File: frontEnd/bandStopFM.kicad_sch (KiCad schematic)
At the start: 18 parts, among them U301 BGS12P2L6E6327XTSA1, U302 BGS12P2L6E6327XTSA1

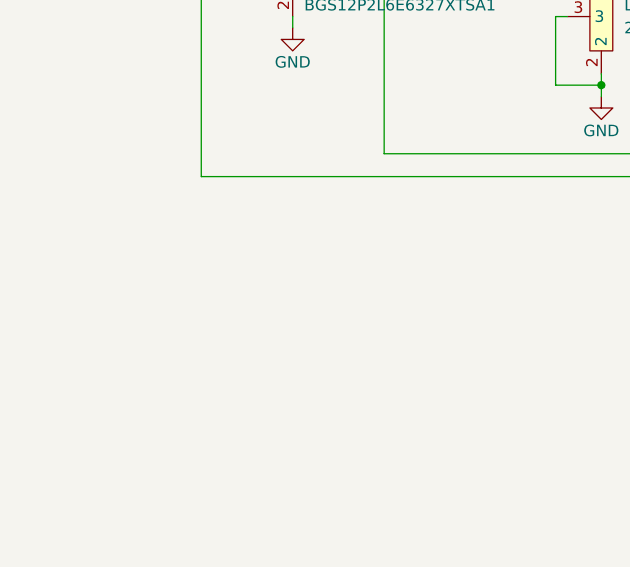
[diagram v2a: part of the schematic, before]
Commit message: add leds for each filter block
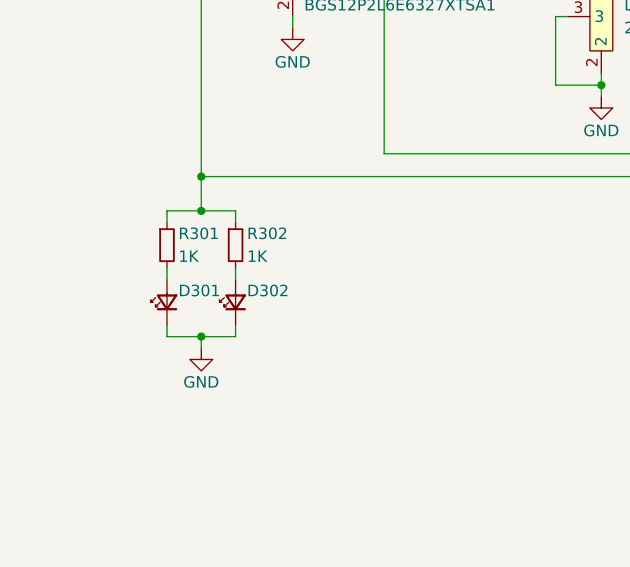
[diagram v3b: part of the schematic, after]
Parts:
- added D301, D302: LED_Small, LED_SMD:LED_0805_2012Metric, symbol Device:LED_Small
- added R301, R302: 1K, Resistor_SMD:R_0805_2012Metric, symbol Device:R_Small
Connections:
- net FILTER_ENABLE: now also R301.1, R302.1
- net GND: now also D301.1 (K), D302.1 (K)
- new net: D301.2 (A), R301.2
- new net: D302.2 (A), R302.2
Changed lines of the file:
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@@
 (kicad_sch (version 20211123) (generator eeschema)
   (paper "A4")
+  (junction (at 58.42 125.73) (diameter 0) (color 0 0 0 0)
+  )
+  (junction (at 58.42 111.76) (diameter 0) (color 0 0 0 0)
+  )
   (junction (at 127 76.2) (diameter 0) (color 0 0 0 0)
   )
@@
   (junction (at 193.04 76.2) (diameter 0) (color 0 0 0 0)
   )
+  (junction (at 58.42 107.95) (diameter 0) (color 0 0 0 0)
+  )
   (junction (at 45.72 167.64) (diameter 0) (color 0 0 0 0)
   )
@@
     (stroke (width 0) (type default) (color 0 0 0 0))
   )
+  (wire (pts (xy 62.23 124.46) (xy 62.23 125.73))
+    (stroke (width 0) (type default) (color 0 0 0 0))
+  )
   (wire (pts (xy 135.89 97.79) (xy 135.89 99.06))
     (stroke (width 0) (type default) (color 0 0 0 0))
@@
     (stroke (width 0) (type default) (color 0 0 0 0))
   )
+  (wire (pts (xy 54.61 125.73) (xy 58.42 125.73))
+    (stroke (width 0) (type default) (color 0 0 0 0))
+  )
   (wire (pts (xy 135.89 82.55) (xy 135.89 83.82))
     (stroke (width 0) (type default) (color 0 0 0 0))
@@
     (stroke (width 0) (type default) (color 0 0 0 0))
   )
+  (wire (pts (xy 54.61 113.03) (xy 54.61 111.76))
+    (stroke (width 0) (type default) (color 0 0 0 0))
+  )
   (wire (pts (xy 119.38 86.36) (xy 119.38 87.63))
     (stroke (width 0) (type default) (color 0 0 0 0))
@@
     (stroke (width 0) (type default) (color 0 0 0 0))
   )
+  (wire (pts (xy 58.42 111.76) (xy 62.23 111.76))
+    (stroke (width 0) (type default) (color 0 0 0 0))
+  )
   (wire (pts (xy 68.58 90.17) (xy 68.58 91.44))
     (stroke (width 0) (type default) (color 0 0 0 0))
@@
     (stroke (width 0) (type default) (color 0 0 0 0))
   )
+  (wire (pts (xy 58.42 125.73) (xy 58.42 127))
+    (stroke (width 0) (type default) (color 0 0 0 0))
+  )
   (wire (pts (xy 227.33 69.85) (xy 227.33 71.12))
     (stroke (width 0) (type default) (color 0 0 0 0))
@@
     (stroke (width 0) (type default) (color 0 0 0 0))
   )
+  (wire (pts (xy 54.61 118.11) (xy 54.61 119.38))
+    (stroke (width 0) (type default) (color 0 0 0 0))
+  )
+  (wire (pts (xy 62.23 118.11) (xy 62.23 119.38))
+    (stroke (width 0) (type default) (color 0 0 0 0))
+  )
   (wire (pts (xy 135.89 96.52) (xy 135.89 97.79))
     (stroke (width 0) (type default) (color 0 0 0 0))
@@
     (stroke (width 0) (type default) (color 0 0 0 0))
   )
+  (wire (pts (xy 54.61 124.46) (xy 54.61 125.73))
+    (stroke (width 0) (type default) (color 0 0 0 0))
+  )
   (wire (pts (xy 97.79 90.17) (xy 97.79 97.79))
     (stroke (width 0) (type default) (color 0 0 0 0))
@@
     (stroke (width 0) (type default) (color 0 0 0 0))
   )
+  (wire (pts (xy 54.61 111.76) (xy 58.42 111.76))
+    (stroke (width 0) (type default) (color 0 0 0 0))
+  )
   (wire (pts (xy 127 76.2) (xy 135.89 76.2))
     (stroke (width 0) (type default) (color 0 0 0 0))
@@
     (stroke (width 0) (type default) (color 0 0 0 0))
   )
+  (wire (pts (xy 58.42 125.73) (xy 62.23 125.73))
+    (stroke (width 0) (type default) (color 0 0 0 0))
+  )
   (wire (pts (xy 102.87 96.52) (xy 102.87 97.79))
     (stroke (width 0) (type default) (color 0 0 0 0))
@@
     (stroke (width 0) (type default) (color 0 0 0 0))
   )
+  (wire (pts (xy 58.42 107.95) (xy 58.42 111.76))
+    (stroke (width 0) (type default) (color 0 0 0 0))
+  )
   (wire (pts (xy 78.74 81.28) (xy 78.74 105.41))
     (stroke (width 0) (type default) (color 0 0 0 0))
@@
   )
   (wire (pts (xy 237.49 107.95) (xy 58.42 107.95))
+    (stroke (width 0) (type default) (color 0 0 0 0))
+  )
+  (wire (pts (xy 62.23 111.76) (xy 62.23 113.03))
     (stroke (width 0) (type default) (color 0 0 0 0))
   )
@@
     )
     (pin "1")
+  )
+  (symbol (lib_id "Device:R_Small") (at 54.61 115.57 0) (unit 1)
+    (in_bom yes) (on_board yes)
+    (property "Reference" "R301" (id 0) (at 55.88 114.3 0)
+      (effects (font (size 1.27 1.27)) (justify left))
+    )
+    (property "Value" "1K" (id 1) (at 55.88 116.84 0)
+      (effects (font (size 1.27 1.27)) (justify left))
+    )
+    (property "Footprint" "Resistor_SMD:R_0805_2012Metric" (id 2) (at 54.61 115.57 0)
+      (effects (font (size 1.27 1.27)) hide)
+    )
+    (property "Datasheet" "~" (id 3) (at 54.61 115.57 0)
+      (effects (font (size 1.27 1.27)) hide)
+    )
+    (pin "1")
+    (pin "2")
   )
   (symbol (lib_id "frontEnd:BGS12P2L6E6327XTSA1") (at 233.68 78.74 0) (mirror y) (unit 1)
@@
     (pin "2")
   )
+  (symbol (lib_id "Device:LED_Small") (at 54.61 121.92 90) (unit 1)
+    (in_bom yes) (on_board yes)
+    (property "Reference" "D301" (id 0) (at 55.88 120.65 90)
+      (effects (font (size 1.27 1.27)) (justify right))
+    )
+    (property "Value" "LED_Small" (id 1) (at 57.15 123.1264 90)
+      (effects (font (size 1.27 1.27)) (justify right) hide)
+    )
+    (property "Footprint" "LED_SMD:LED_0805_2012Metric" (id 2) (at 54.61 121.92 90)
+      (effects (font (size 1.27 1.27)) hide)
+    )
+    (property "Datasheet" "~" (id 3) (at 54.61 121.92 90)
+      (effects (font (size 1.27 1.27)) hide)
+    )
+    (pin "1")
+    (pin "2")
+  )
   (symbol (lib_id "Device:C_Small") (at 41.91 171.45 180) (unit 1)
     (in_bom yes) (on_board yes)
@@
     )
     (property "Datasheet" "~" (id 3) (at 135.89 80.01 0)
+      (effects (font (size 1.27 1.27)) hide)
+    )
+    (pin "1")
+    (pin "2")
+  )
+  (symbol (lib_id "Device:LED_Small") (at 62.23 121.92 90) (unit 1)
+    (in_bom yes) (on_board yes)
+    (property "Reference" "D302" (id 0) (at 63.5 120.65 90)
+      (effects (font (size 1.27 1.27)) (justify right))
+    )
+    (property "Value" "LED_Small" (id 1) (at 64.77 123.1264 90)
+      (effects (font (size 1.27 1.27)) (justify right) hide)
+    )
+    (property "Footprint" "LED_SMD:LED_0805_2012Metric" (id 2) (at 62.23 121.92 90)
+      (effects (font (size 1.27 1.27)) hide)
+    )
+    (property "Datasheet" "~" (id 3) (at 62.23 121.92 90)
       (effects (font (size 1.27 1.27)) hide)
     )
@@
       (effects (font (size 1.27 1.27)) hide)
     )
+    (pin "1")
+    (pin "2")
+  )
+  (symbol (lib_id "power:GND") (at 58.42 127 0) (unit 1)
+    (in_bom yes) (on_board yes)
+    (property "Reference" "#PWR?" (id 0) (at 58.42 133.35 0)
+      (effects (font (size 1.27 1.27)) hide)
+    )
+    (property "Value" "GND" (id 1) (at 58.42 130.81 0))
+    (property "Footprint" "" (id 2) (at 58.42 127 0)
+      (effects (font (size 1.27 1.27)) hide)
+    )
+    (property "Datasheet" "" (id 3) (at 58.42 127 0)
+      (effects (font (size 1.27 1.27)) hide)
+    )
+    (pin "1")
+  )
+  (symbol (lib_id "Device:R_Small") (at 62.23 115.57 0) (unit 1)
+    (in_bom yes) (on_board yes)
+    (property "Reference" "R302" (id 0) (at 63.5 114.3 0)
+      (effects (font (size 1.27 1.27)) (justify left))
+    )
+    (property "Value" "1K" (id 1) (at 63.5 116.84 0)
+      (effects (font (size 1.27 1.27)) (justify left))
+    )
+    (property "Footprint" "Resistor_SMD:R_0805_2012Metric" (id 2) (at 62.23 115.57 0)
+      (effects (font (size 1.27 1.27)) hide)
+    )
+    (property "Datasheet" "~" (id 3) (at 62.23 115.57 0)
+      (effects (font (size 1.27 1.27)) hide)
+    )

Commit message: assign footprints, part designators
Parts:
- U301, U302: footprint (none) -> frontEnd:BGS12P2L6E6327XTSA1
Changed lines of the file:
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@@
   (symbol (lib_id "power:GND") (at 201.93 99.06 0) (unit 1)
     (in_bom yes) (on_board yes)
-    (property "Reference" "#PWR?" (id 0) (at 201.93 105.41 0)
+    (property "Reference" "#PWR0156" (id 0) (at 201.93 105.41 0)
       (effects (font (size 1.27 1.27)) hide)
     )
@@
       (effects (font (size 1.27 1.27)) (justify right))
     )
-    (property "Footprint" "" (id 2) (at 233.68 78.74 0)
+    (property "Footprint" "frontEnd:BGS12P2L6E6327XTSA1" (id 2) (at 233.68 78.74 0)
       (effects (font (size 1.27 1.27)) hide)
     )
@@
   (symbol (lib_id "power:GND") (at 119.38 87.63 0) (unit 1)
     (in_bom yes) (on_board yes)
-    (property "Reference" "#PWR?" (id 0) (at 119.38 93.98 0)
+    (property "Reference" "#PWR0148" (id 0) (at 119.38 93.98 0)
       (effects (font (size 1.27 1.27)) hide)
     )
@@
   (symbol (lib_id "power:GND") (at 135.89 99.06 0) (unit 1)
     (in_bom yes) (on_board yes)
-    (property "Reference" "#PWR?" (id 0) (at 135.89 105.41 0)
+    (property "Reference" "#PWR0150" (id 0) (at 135.89 105.41 0)
       (effects (font (size 1.27 1.27)) hide)
     )
@@
   (symbol (lib_id "power:+3V3") (at 227.33 69.85 0) (unit 1)
     (in_bom yes) (on_board yes)
-    (property "Reference" "#PWR?" (id 0) (at 227.33 73.66 0)
+    (property "Reference" "#PWR0155" (id 0) (at 227.33 73.66 0)
       (effects (font (size 1.27 1.27)) hide)
     )
@@
   (symbol (lib_id "power:GND") (at 152.4 87.63 0) (unit 1)
     (in_bom yes) (on_board yes)
-    (property "Reference" "#PWR?" (id 0) (at 152.4 93.98 0)
+    (property "Reference" "#PWR0149" (id 0) (at 152.4 93.98 0)
       (effects (font (size 1.27 1.27)) hide)
     )
@@
   (symbol (lib_id "power:GND") (at 168.91 99.06 0) (unit 1)
     (in_bom yes) (on_board yes)
-    (property "Reference" "#PWR?" (id 0) (at 168.91 105.41 0)
+    (property "Reference" "#PWR0152" (id 0) (at 168.91 105.41 0)
       (effects (font (size 1.27 1.27)) hide)
     )
@@
   (symbol (lib_id "power:GND") (at 227.33 91.44 0) (unit 1)
     (in_bom yes) (on_board yes)
-    (property "Reference" "#PWR?" (id 0) (at 227.33 97.79 0)
+    (property "Reference" "#PWR0154" (id 0) (at 227.33 97.79 0)
       (effects (font (size 1.27 1.27)) hide)
     )
@@
   (symbol (lib_id "power:GND") (at 68.58 91.44 0) (unit 1)
     (in_bom yes) (on_board yes)
-    (property "Reference" "#PWR?" (id 0) (at 68.58 97.79 0)
+    (property "Reference" "#PWR0157" (id 0) (at 68.58 97.79 0)
       (effects (font (size 1.27 1.27)) hide)
     )
@@
   (symbol (lib_id "power:GND") (at 45.72 176.53 0) (unit 1)
     (in_bom yes) (on_board yes)
-    (property "Reference" "#PWR?" (id 0) (at 45.72 182.88 0)
+    (property "Reference" "#PWR0160" (id 0) (at 45.72 182.88 0)
       (effects (font (size 1.27 1.27)) hide)
     )
@@
   (symbol (lib_id "power:+3V3") (at 45.72 166.37 0) (unit 1)
     (in_bom yes) (on_board yes)
-    (property "Reference" "#PWR?" (id 0) (at 45.72 170.18 0)
+    (property "Reference" "#PWR0161" (id 0) (at 45.72 170.18 0)
       (effects (font (size 1.27 1.27)) hide)
     )
@@
   (symbol (lib_id "power:GND") (at 185.42 87.63 0) (unit 1)
     (in_bom yes) (on_board yes)
-    (property "Reference" "#PWR?" (id 0) (at 185.42 93.98 0)
+    (property "Reference" "#PWR0153" (id 0) (at 185.42 93.98 0)
       (effects (font (size 1.27 1.27)) hide)
     )
@@
   (symbol (lib_id "power:GND") (at 102.87 99.06 0) (unit 1)
     (in_bom yes) (on_board yes)
-    (property "Reference" "#PWR?" (id 0) (at 102.87 105.41 0)
+    (property "Reference" "#PWR0151" (id 0) (at 102.87 105.41 0)
       (effects (font (size 1.27 1.27)) hide)
     )
@@
       (effects (font (size 1.27 1.27)) (justify left))
     )
-    (property "Footprint" "" (id 2) (at 62.23 78.74 0)
+    (property "Footprint" "frontEnd:BGS12P2L6E6327XTSA1" (id 2) (at 62.23 78.74 0)
       (effects (font (size 1.27 1.27)) hide)
     )
@@
   (symbol (lib_id "power:+3V3") (at 68.58 69.85 0) (unit 1)
     (in_bom yes) (on_board yes)
-    (property "Reference" "#PWR?" (id 0) (at 68.58 73.66 0)
+    (property "Reference" "#PWR0158" (id 0) (at 68.58 73.66 0)
       (effects (font (size 1.27 1.27)) hide)
     )
@@
   (symbol (lib_id "power:GND") (at 58.42 127 0) (unit 1)
     (in_bom yes) (on_board yes)
-    (property "Reference" "#PWR?" (id 0) (at 58.42 133.35 0)
-      (effects (font (size 1.27 1.27)) hide)
-    )
+    (property "Reference" "#PWR0159" (id 0) (at 58.42 133.35 0)
+      (effects (font (size 1.27 1.27)) hide)
+    )

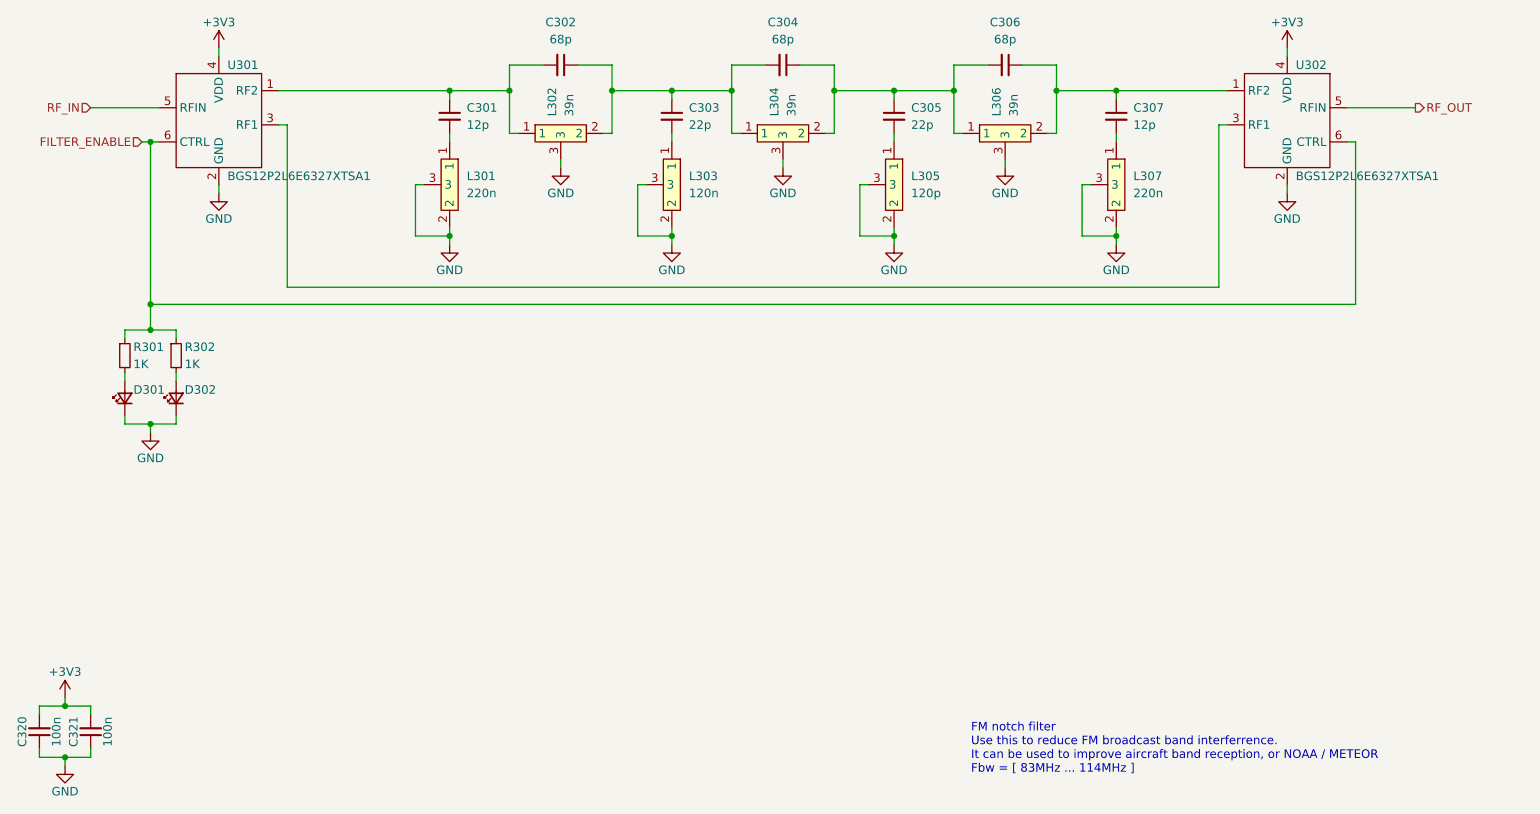
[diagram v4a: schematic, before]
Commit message: convert all embeded filter to plug-in modules, start pcb layout
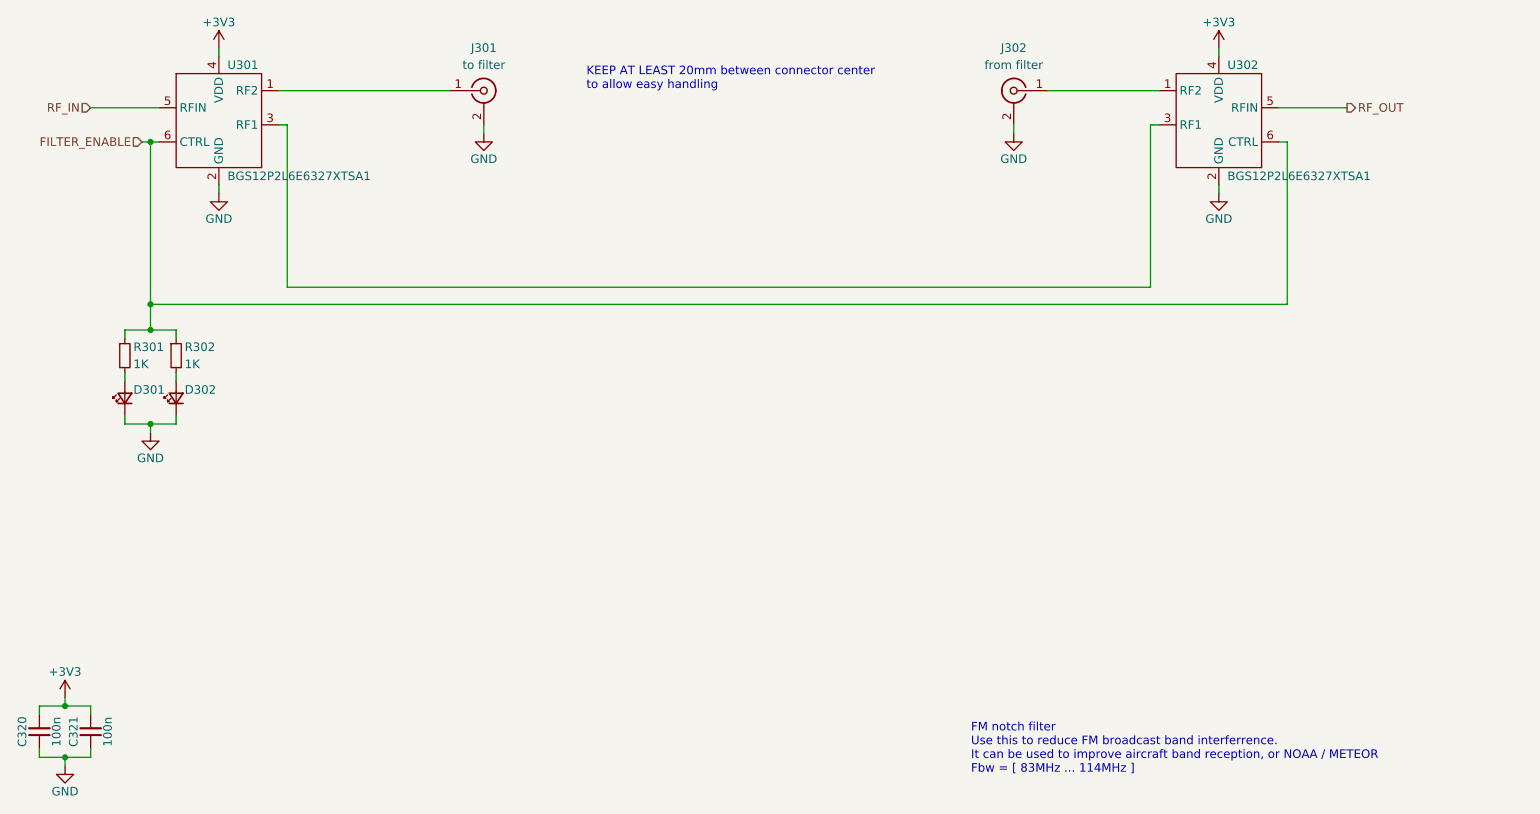
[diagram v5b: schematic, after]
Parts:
- removed C301, C307: 12p, Capacitor_SMD:C_0805_2012Metric, symbol Device:C_Small
- removed C302, C304, C306: 68p, Capacitor_SMD:C_0805_2012Metric, symbol Device:C_Small
- removed C303, C305: 22p, Capacitor_SMD:C_0805_2012Metric, symbol Device:C_Small
- removed L301, L307: 220n, frontEnd:COIL, symbol frontEnd:DIY_COIL
- removed L302, L304, L306: 39n, frontEnd:COIL, symbol frontEnd:DIY_COIL
- removed L303: 120n, frontEnd:COIL, symbol frontEnd:DIY_COIL
- removed L305: 120p, frontEnd:COIL, symbol frontEnd:DIY_COIL
- added J301: to filter, frontEnd:SMA_FEM_TH_VERTICAL, symbol Connector:Conn_Coaxial
- added J302: from filter, frontEnd:SMA_FEM_TH_VERTICAL, symbol Connector:Conn_Coaxial
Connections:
- net GND: now also J301.2 (Ext), J302.2 (Ext)
- net at U302.1 (RF2): now also J302.1 (In)
- net at U301.1 (RF2): now also J301.1 (In)
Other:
- note added: "KEEP AT LEAST 20mm between connector center to allow easy handling"
- moved on the sheet: U302
